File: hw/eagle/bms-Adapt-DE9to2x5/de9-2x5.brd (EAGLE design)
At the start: 44.9 x 37.7 mm, 8 parts

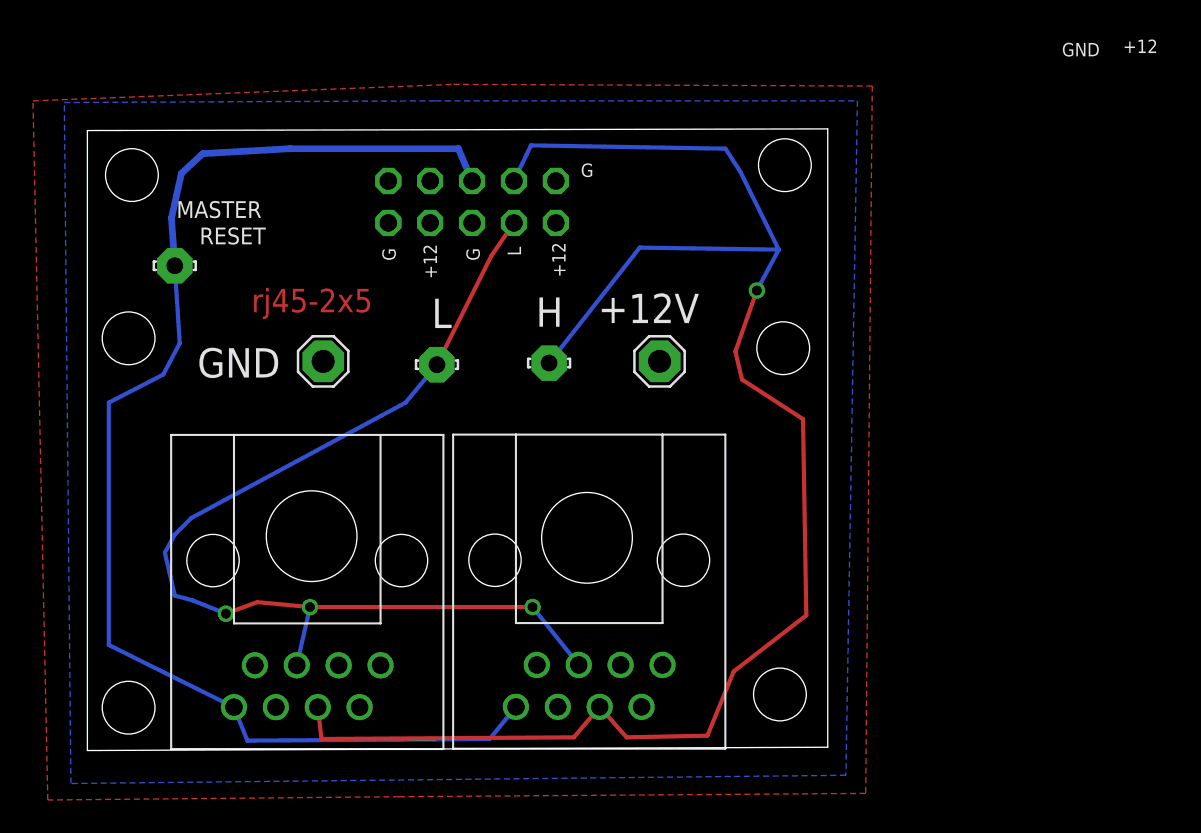
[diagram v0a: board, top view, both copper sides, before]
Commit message: save suboard eagle file
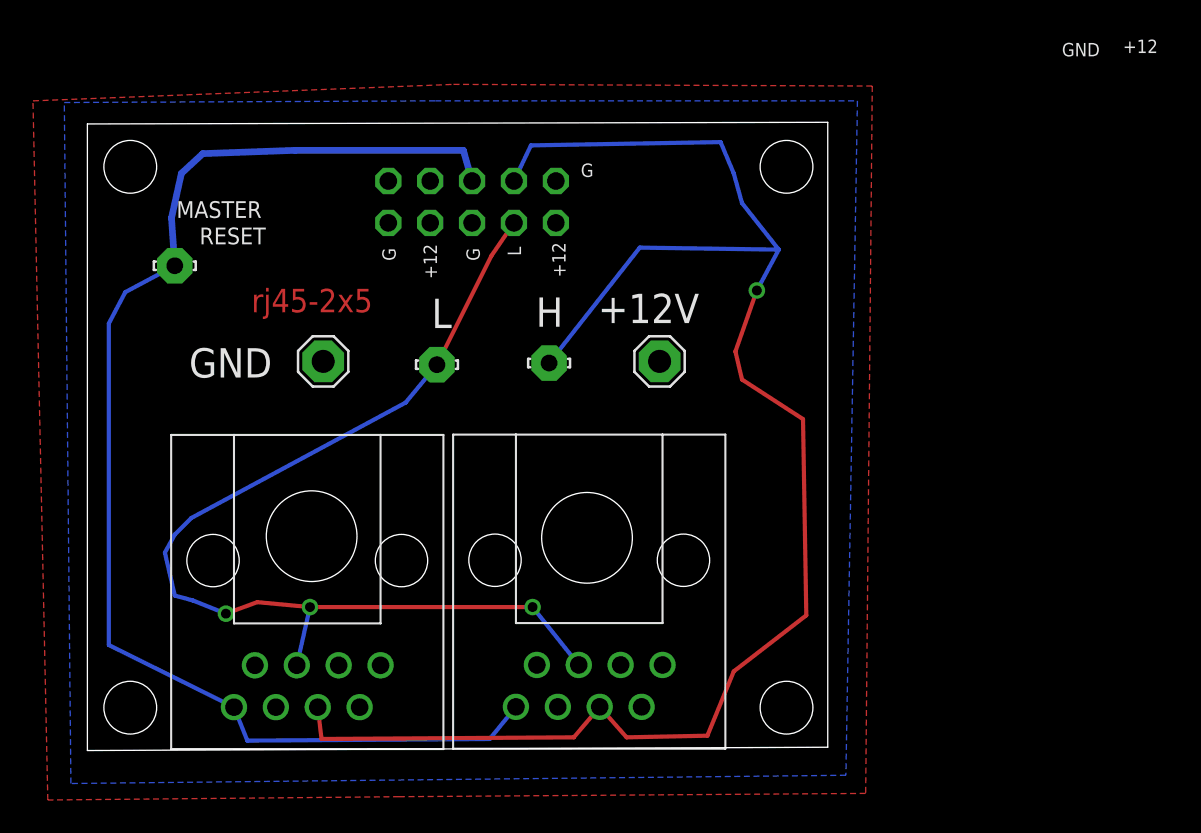
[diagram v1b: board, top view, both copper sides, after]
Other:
- board size 44.9 x 37.7 mm -> 44.9 x 38.1 mm
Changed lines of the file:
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@@
 <plain>
 <wire x1="0" y1="0" x2="44.9" y2="0.2" width="0" layer="20"/>
-<wire x1="44.9" y1="0.2" x2="44.9" y2="37.7" width="0" layer="20"/>
-<wire x1="44.9" y1="37.7" x2="0" y2="37.6" width="0" layer="20"/>
-<wire x1="0" y1="37.6" x2="0" y2="0" width="0" layer="20"/>
+<wire x1="44.9" y1="0.2" x2="44.9" y2="38.1" width="0" layer="20"/>
+<wire x1="44.9" y1="38.1" x2="0" y2="38" width="0" layer="20"/>
+<wire x1="0" y1="38" x2="0" y2="0" width="0" layer="20"/>
 <text x="28.7" y="27.5" size="1.778" layer="26" rot="MR180">H</text>
 <text x="21.5" y="27.4" size="1.778" layer="26" rot="MR180">L</text>
@@
 <text x="5.4" y="32.3" size="1.016" layer="25">MASTER</text>
 <text x="6.8" y="30.7" size="1.016" layer="25">RESET</text>
-<text x="11.7" y="24.4" size="1.778" layer="25" rot="R180">GND</text>
+<text x="11.2" y="24.4" size="1.778" layer="25" rot="R180">GND</text>
 <text x="37.1" y="27.7" size="1.778" layer="25" rot="R180">+12V</text>
-<hole x="2.7" y="34.9" drill="3.2"/>
-<hole x="2.5" y="2.6" drill="3.2"/>
-<hole x="42.3" y="35.5" drill="3.2"/>
-<hole x="42" y="3.4" drill="3.2"/>
 <text x="59.1" y="42.1" size="0.8128" layer="25">GND</text>
 <text x="62.8" y="42.3" size="0.8128" layer="25">+12</text>
@@
 <hole x="13.6" y="13" drill="5.5"/>
 <hole x="30.3" y="12.9" drill="5.5"/>
-<hole x="2.5" y="25" drill="3.2"/>
-<hole x="42.2" y="24.4" drill="3.2"/>
+<hole x="2.6" y="2.6" drill="3.2"/>
+<hole x="2.6" y="35.4" drill="3.2"/>
+<hole x="42.4" y="35.4" drill="3.2"/>
+<hole x="42.4" y="2.6" drill="3.2"/>
 </plain>
 <attributes>
@@
 <wire x1="14.2" y1="0.7" x2="13.97" y2="2.63" width="0.254" layer="1"/>
 <wire x1="25.87" y1="34.54" x2="26.9" y2="36.7" width="0.254" layer="16"/>
-<wire x1="26.9" y1="36.7" x2="38.7" y2="36.5" width="0.254" layer="16"/>
-<wire x1="38.7" y1="36.5" x2="39.6" y2="35.1" width="0.254" layer="16"/>
-<wire x1="39.6" y1="35.1" x2="41.93060625" y2="30.3779375" width="0.254" layer="16"/>
+<wire x1="26.9" y1="36.7" x2="38.4" y2="36.9" width="0.254" layer="16"/>
+<wire x1="38.4" y1="36.9" x2="39.2" y2="35" width="0.254" layer="16"/>
+<wire x1="39.2" y1="35" x2="39.7" y2="33.2" width="0.254" layer="16"/>
+<wire x1="39.7" y1="33.2" x2="41.93060625" y2="30.3779375" width="0.254" layer="16"/>
 <wire x1="41.93060625" y1="30.3779375" x2="33.5" y2="30.5" width="0.254" layer="16"/>
 <wire x1="33.5" y1="30.5" x2="28" y2="23.5" width="0.254" layer="16"/>
@@
 <wire x1="5.1" y1="32.3" x2="5.7" y2="35" width="0.4064" layer="16"/>
 <wire x1="5.7" y1="35" x2="7" y2="36.2" width="0.4064" layer="16"/>
-<wire x1="7" y1="36.2" x2="12.3" y2="36.5" width="0.4064" layer="16"/>
-<wire x1="12.3" y1="36.5" x2="22.5" y2="36.5" width="0.4064" layer="16"/>
-<wire x1="22.5" y1="36.5" x2="23.33" y2="34.54" width="0.4064" layer="16"/>
+<wire x1="7" y1="36.2" x2="12.6" y2="36.4" width="0.4064" layer="16"/>
+<wire x1="12.6" y1="36.4" x2="22.8" y2="36.4" width="0.4064" layer="16"/>
+<wire x1="22.8" y1="36.4" x2="23.33" y2="34.54" width="0.4064" layer="16"/>
 <wire x1="8.89" y1="2.63" x2="1.3" y2="6.4" width="0.254" layer="16"/>
-<wire x1="1.3" y1="6.4" x2="1.3" y2="21.1" width="0.254" layer="16"/>
-<wire x1="1.3" y1="21.1" x2="4.6" y2="22.8" width="0.254" layer="16"/>
-<wire x1="4.6" y1="22.8" x2="5.6" y2="24.7" width="0.254" layer="16"/>
-<wire x1="5.6" y1="24.7" x2="5.3" y2="29.4" width="0.254" layer="16"/>
+<wire x1="1.3" y1="6.4" x2="1.3" y2="25.9" width="0.254" layer="16"/>
+<wire x1="1.3" y1="25.9" x2="2.3" y2="27.8" width="0.254" layer="16"/>
+<wire x1="2.3" y1="27.8" x2="5.3" y2="29.4" width="0.254" layer="16"/>
 <wire x1="8.89" y1="2.63" x2="9.7" y2="0.6" width="0.254" layer="16"/>
 <wire x1="9.7" y1="0.6" x2="24.4" y2="0.7" width="0.254" layer="16"/>

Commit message: bms-Adapt-DE9to2x5 sub-board eagle file update
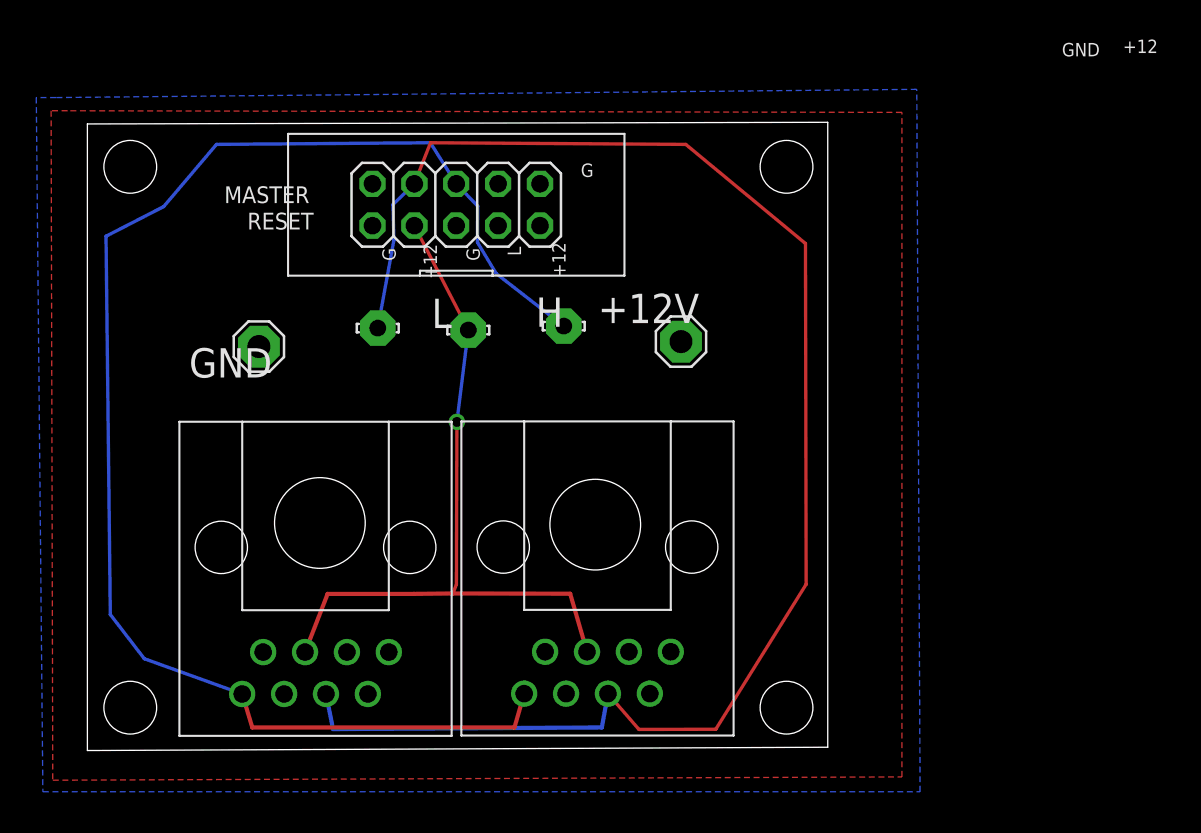
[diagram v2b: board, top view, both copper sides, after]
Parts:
- moved LSP5 23.9 mm to (28.9, 25.7)
- moved LSP2 10.6 mm to (17.6, 25.6)
- moved LSP4 4.00 mm to (10.4, 24.5)
- moved LSP6 2.83 mm to (23.1, 25.5)
- moved LSP1 1.77 mm to (36.0, 24.8)
- moved JP6 0.97 mm to (22.4, 33.1), flipped to the top
- moved JP7 0.94 mm to (14.5, 3.43)
- moved JP8 0.94 mm to (31.6, 3.45)
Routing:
- net CANL: track 63.0 -> 45.3 mm, vias 3 -> 1
- net MASTER-RESET-SYS: track 78.1 -> 89.1 mm
- net CANH: track 100.4 -> 96.1 mm, vias 1 -> 0
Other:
- board text added: "M.Reset"
- board text removed: "rj45-2x5"

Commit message: bms sub-board ready and gerber checked
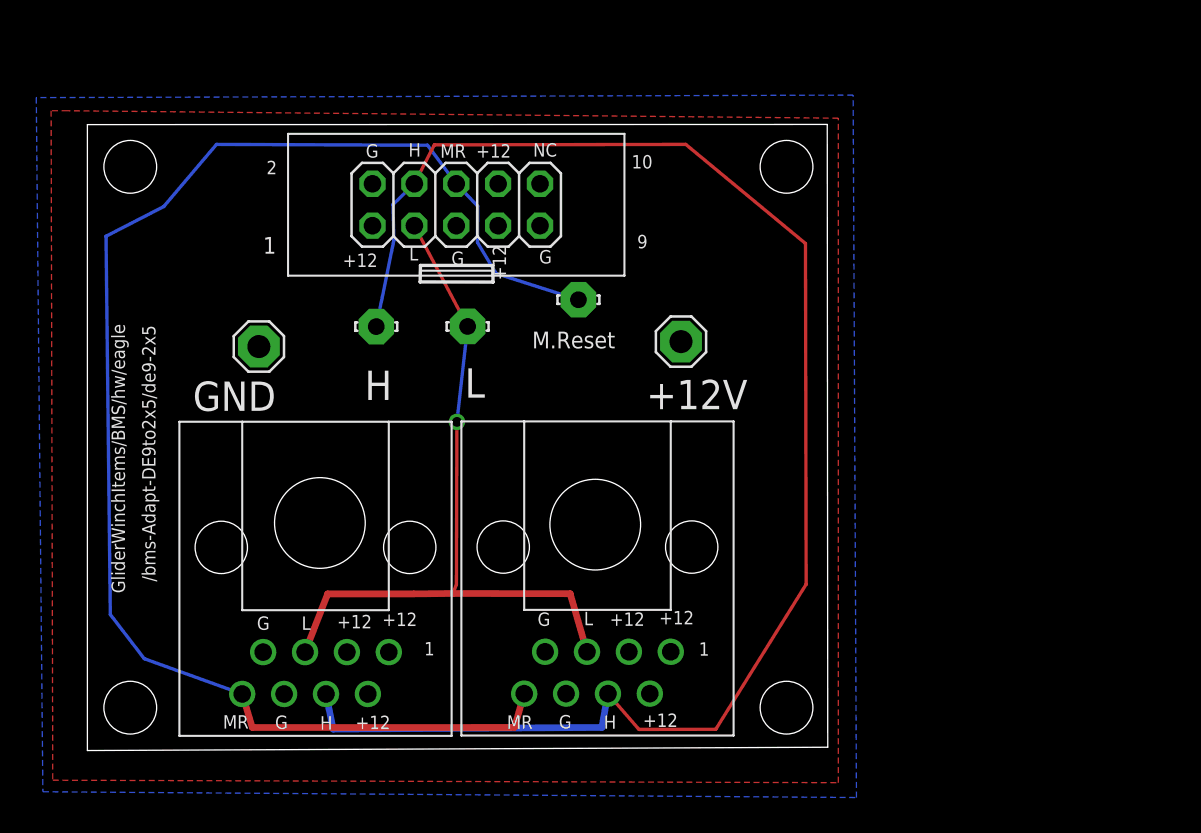
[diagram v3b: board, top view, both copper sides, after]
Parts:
- moved LSP5 1.83 mm to (29.8, 27.3)
- moved LSP6 0.22 mm to (23.1, 25.7)
- moved LSP2 0.13 mm to (17.5, 25.7)
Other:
- board size 44.9 x 38.1 mm -> 44.9 x 38 mm
- board text added: "/bms-Adapt-DE9to2x5/de9-2x5"
- board text added: "10"
- board text added: "2"
- board text added: "9"
- board text added: "GliderWinchItems/BMS/hw/eagle"
- board text added: "MR"
- board text added: "NC"
- board text removed: "CAN"
- board text removed: "MASTER"
- board text removed: "RESET"
